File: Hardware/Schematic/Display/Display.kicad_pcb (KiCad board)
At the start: 2 copper layers, 17 parts, among them J10 Conn_01x02, J8 Conn_01x24, Q1 Q_PJFET_GSD

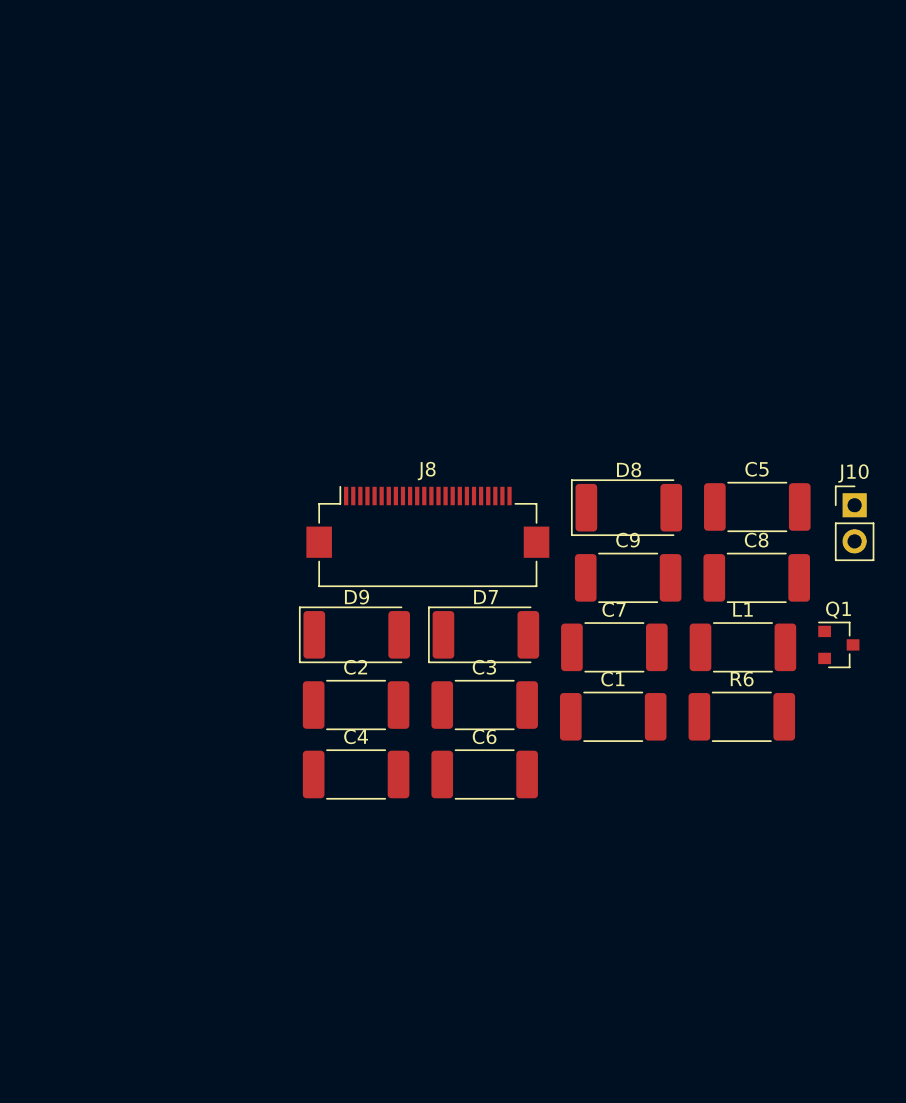
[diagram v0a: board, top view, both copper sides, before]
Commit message: Updated keypad and display schematic to use header sockets for intra-board connections.
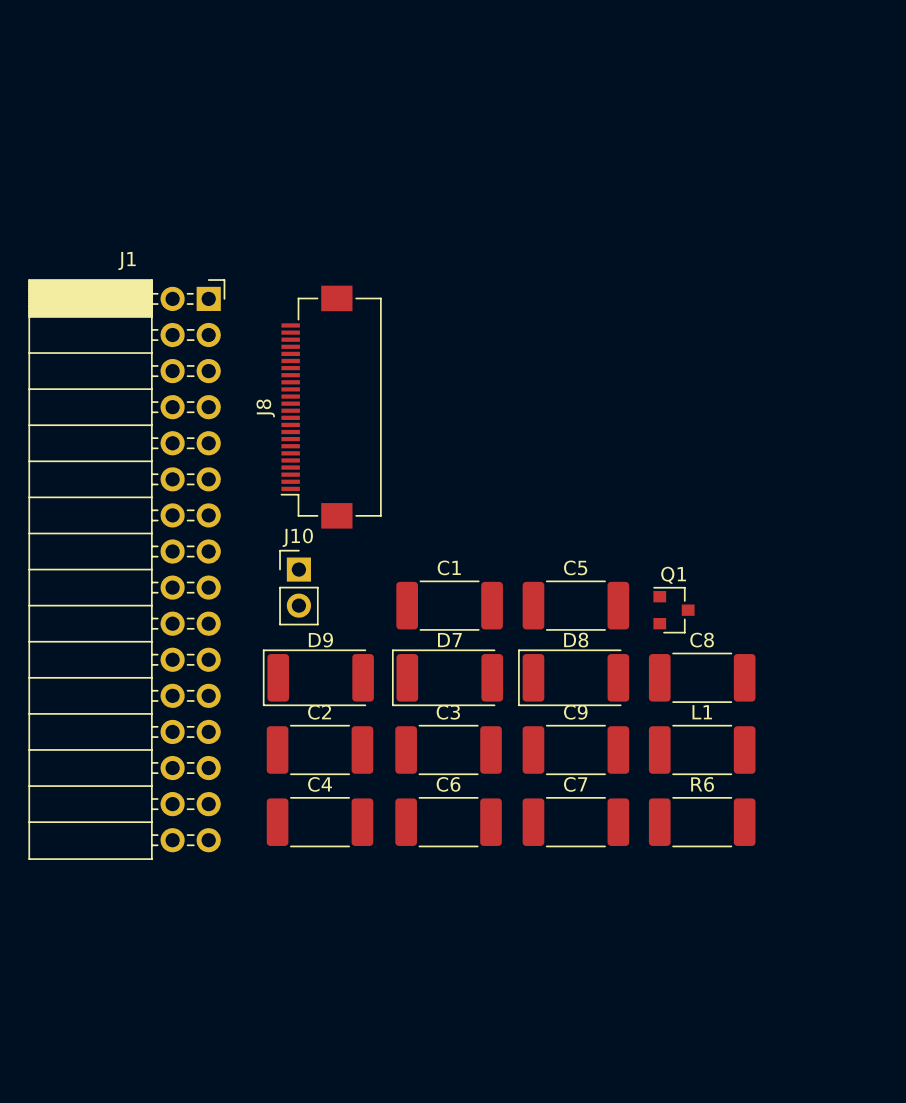
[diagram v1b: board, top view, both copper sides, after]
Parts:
- added J1: Conn_01x32, Connector_PinSocket_2.54mm:PinSocket_2x16_P2.54mm_Horizontal, F.Cu at (123.2, 71.1)
- moved J10 39.4 mm to (129.5, 90.2)
- moved C5 14.5 mm to (149.0, 92.7)
- moved C1 13.9 mm to (140.1, 92.7)
- moved C9 12.7 mm to (149.0, 102.9)
- moved C7 12.6 mm to (149.0, 108.0)
- moved D8 12.5 mm to (149.0, 97.8)
- moved Q1 11.9 mm to (155.9, 93.0)
- moved J8 11.3 mm to (130.8, 78.7), turned to 90 degrees
- moved C8 8.01 mm to (157.9, 97.8)
- moved R6 7.92 mm to (157.9, 108.0)
- moved L1 7.77 mm to (157.9, 102.9)
- moved C6 4.21 mm to (140.1, 108.0)
- moved C4 4.21 mm to (131.0, 108.0)
- moved C3 4.06 mm to (140.1, 102.9)
- moved C2 4.06 mm to (131.0, 102.9)
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
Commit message: Added male 02x16 header to auxillary boards so they can be "stacked" together
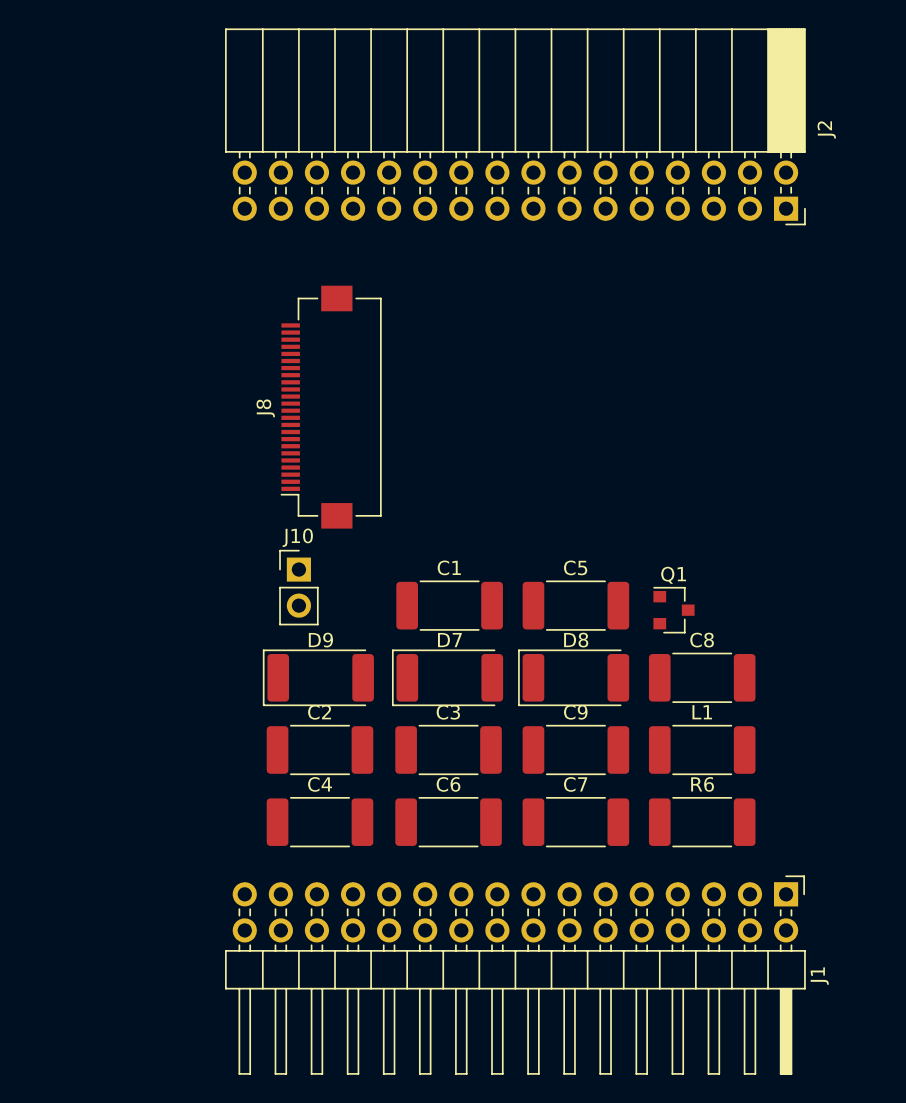
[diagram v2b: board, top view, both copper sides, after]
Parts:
- added J2: Conn_01x32, Connector_PinSocket_2.54mm:PinSocket_2x16_P2.54mm_Horizontal, F.Cu at (163.8, 64.8)
- J1: footprint Connector_PinSocket_2.54mm:PinSocket_2x16_P2.54mm_Horizontal -> Connector_PinHeader_2.54mm:PinHeader_2x16_P2.54mm_Horizontal
- moved J1 58.4 mm to (163.8, 113.0), turned to 270 degrees
